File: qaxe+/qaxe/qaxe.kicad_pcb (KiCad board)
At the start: 4 copper layers, 89 x 137 mm, 223 parts, among them J1 Barrel_Jack_Switch, J2 Conn_01x06, J3 SWD, J4 Conn_01x02, J5 Conn_01x02, J6 USB_C_Receptacle_USB2.0, M1 Fan_4pin, M2 Fan_4pin, Q3 CSD16415Q5T, Q4 CSD16415Q5T, Q5 CSD16415Q5T, Q6 CSD16415Q5T, Q7 BSS138, SW1 boot, U19 BM1368_mode1, U20 BM1368_mode1, U25 BM1368_mode1, U26 BM1368_mode1, U29 TXU0101, U3 LTC3856, U32 TMP1075, U33 TMP1075, U35 STM32L072CBT6, U36 1117-3.3, U37 TXU0101, U38 TXU0101, U39 TXU0101, U4 MCP1824T-0802E, U6 AP3211, U7 MCP1824T-1802E, U8 25MHz, X1 8MHz

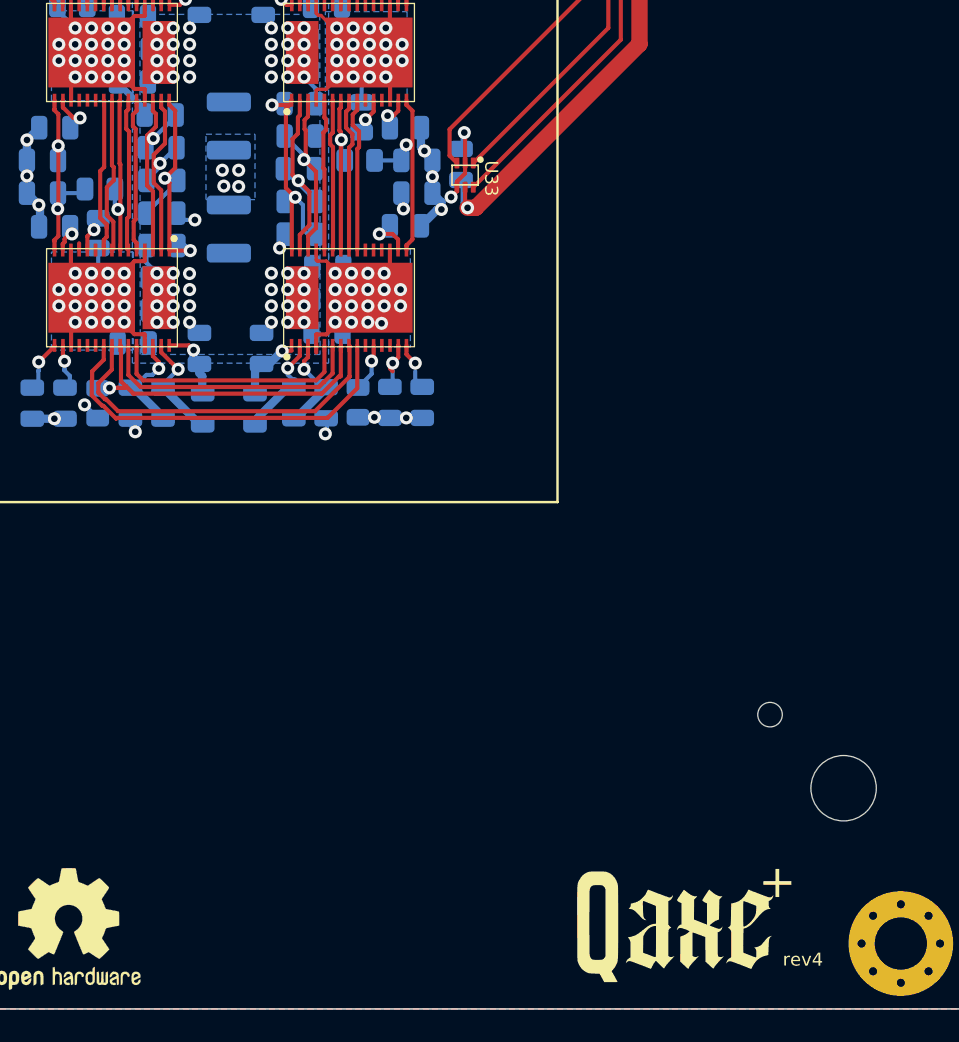
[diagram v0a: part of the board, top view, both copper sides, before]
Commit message: rev4.1 qaxe+ (added pull downs on NRSTI)
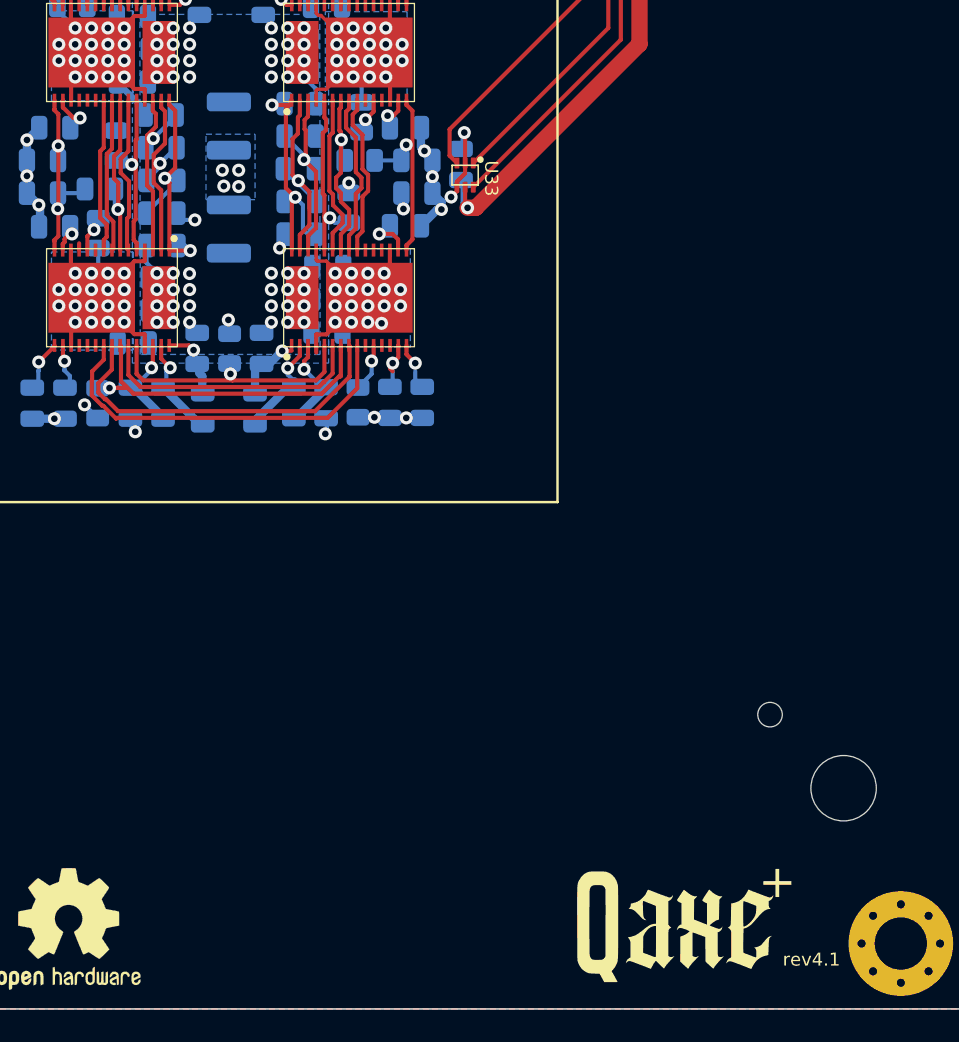
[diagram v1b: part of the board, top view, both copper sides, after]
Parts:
- added R49: 10k, Resistor_SMD:R_0805_2012Metric, B.Cu at (88.0, 123.2)
- added R50: 10k, Resistor_SMD:R_0805_2012Metric, B.Cu at (94.9, 135.6)
- added R51: 10k, Resistor_SMD:R_0805_2012Metric, B.Cu at (102.2, 127.0)
- moved C73 0.14 mm to (93.0, 135.6)
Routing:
- net GND: track 276.5 -> 270.7 mm, vias 252 -> 254
- net Net-(U20-NRSTO): track 9.31 -> 11.0 mm, vias 0 -> 1
- net Net-(U20-NRSTI): track 15.2 -> 16.3 mm, vias 0 -> 1
- net Net-(U19-NRSTO): track 9.46 -> 10.4 mm, vias 0 -> 1
- net Net-(U20-RI): track 10.6 -> 11.3 mm
- net Net-(U20-CO): track 9.32 -> 9.84 mm
- net Net-(U25-VDD1_1): track 6.37 -> 5.86 mm
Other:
- board text added: "rev4.1"
- board text removed: "rev4"
